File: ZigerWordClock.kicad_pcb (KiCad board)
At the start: 2 copper layers, 237 x 237 mm, 19 parts, among them U1 BTF-5V-060L-B_SK9822_LED_Stri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, U10 BTF-5V-060L-B_SK9822_LED_Stri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, U11 BTF-5V-060L-B_SK9822_LED_Stri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, U12 BTF-5V-060L-B_SK9822_LED_Stri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, U13 BTF-5V-060L-B_SK9822_LED_Stri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, U14 BTF-5V-060L-B_SK9822_LED_Stri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, U15 BTF-5V-060L-B_SK9822_LED_Stri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, U16 BTF-5V-060L-B_SK9822_LED_Stri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, U17 BH1750, U18 LILYGO(R)_TTGO_T8_ESP32-S2_V1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, U19 LevelShifter, U2 BTF-5V-060L-B_SK9822_LED_Stri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, U3 BTF-5V-060L-B_SK9822_LED_Stri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, U4 BTF-5V-060L-B_SK9822_LED_Stri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, U5 BTF-5V-060L-B_SK9822_LED_Stri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, U6 BTF-5V-060L-B_SK9822_LED_Stri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, U7 BTF-5V-060L-B_SK9822_LED_Stri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, U8 BTF-5V-060L-B_SK9822_LED_Stri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, U9 BTF-5V-060L-B_SK9822_LED_Stri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

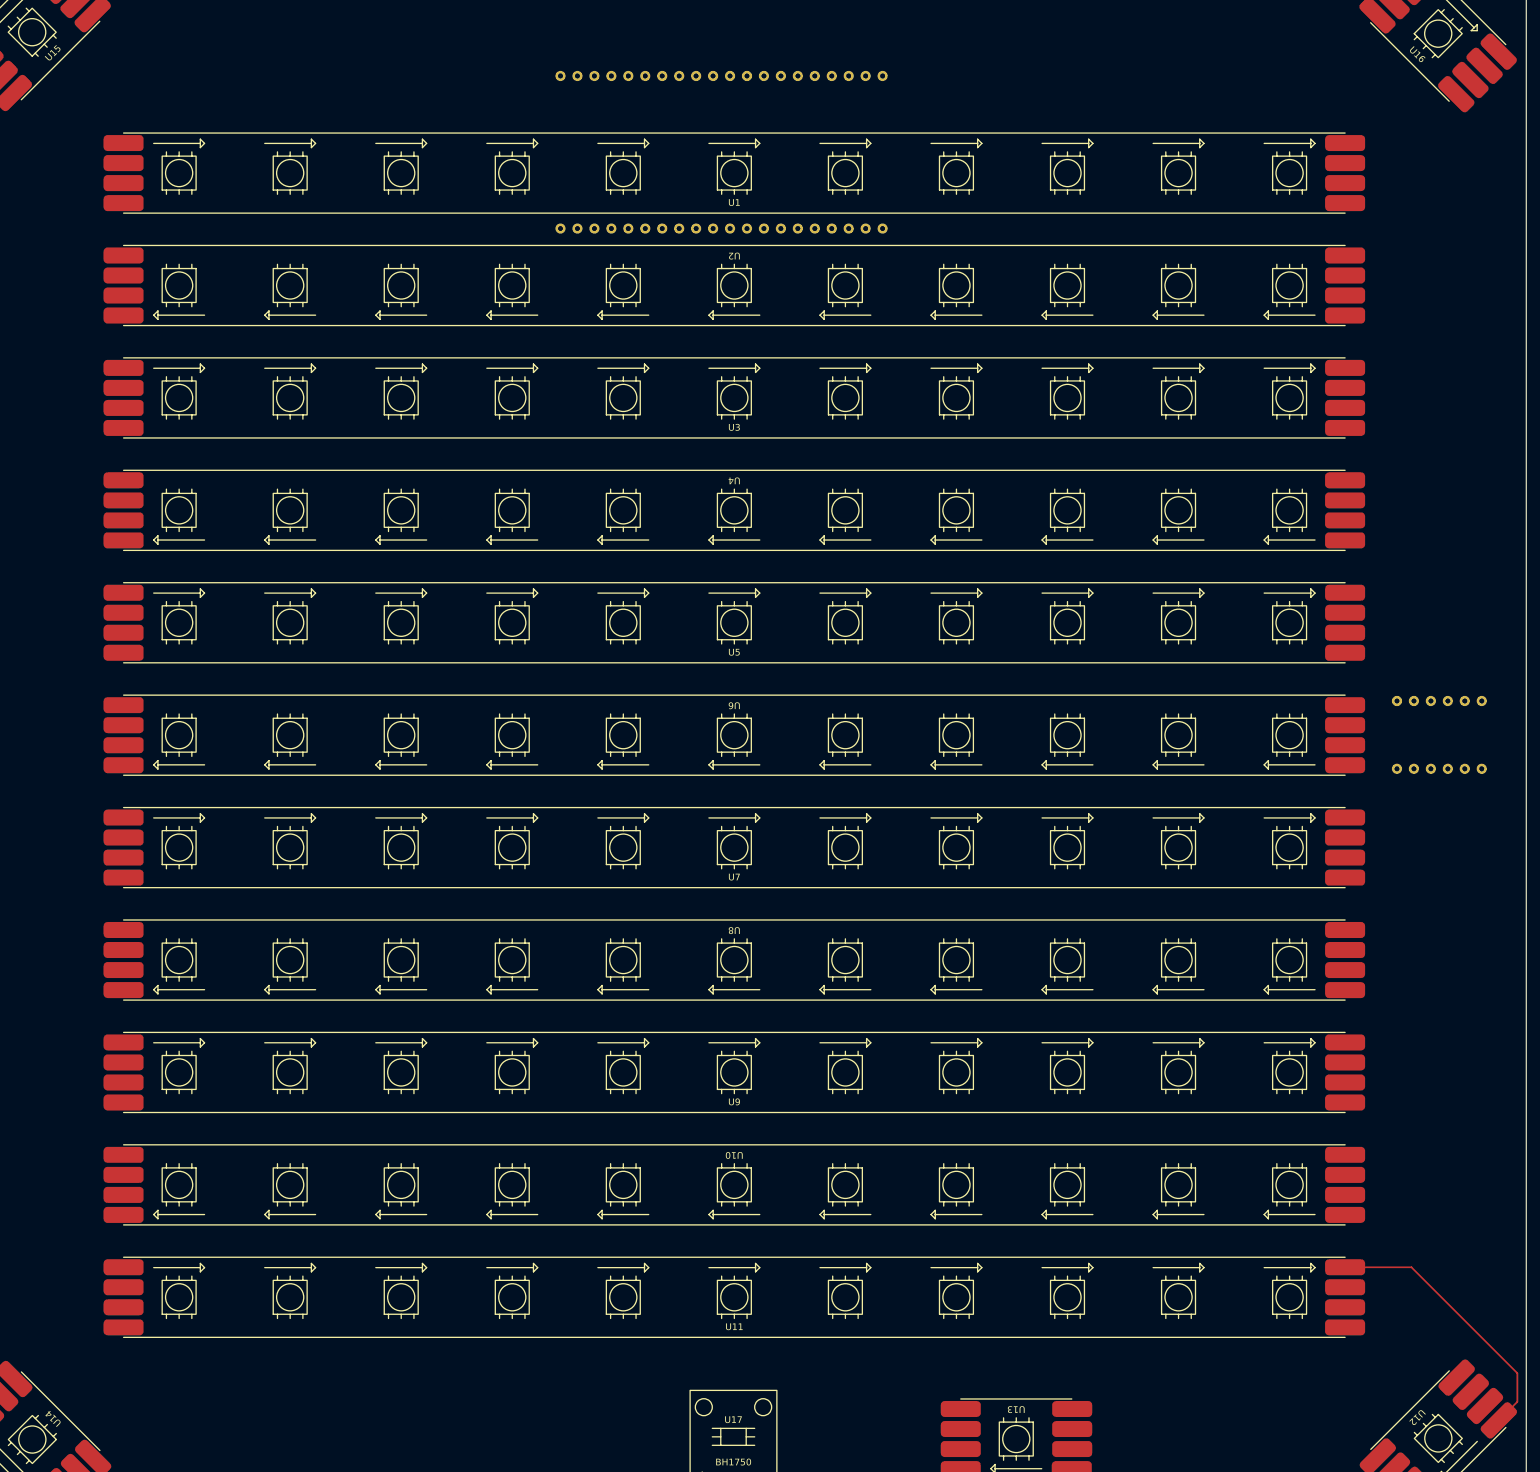
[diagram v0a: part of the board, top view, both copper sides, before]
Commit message: Pins fixed in library
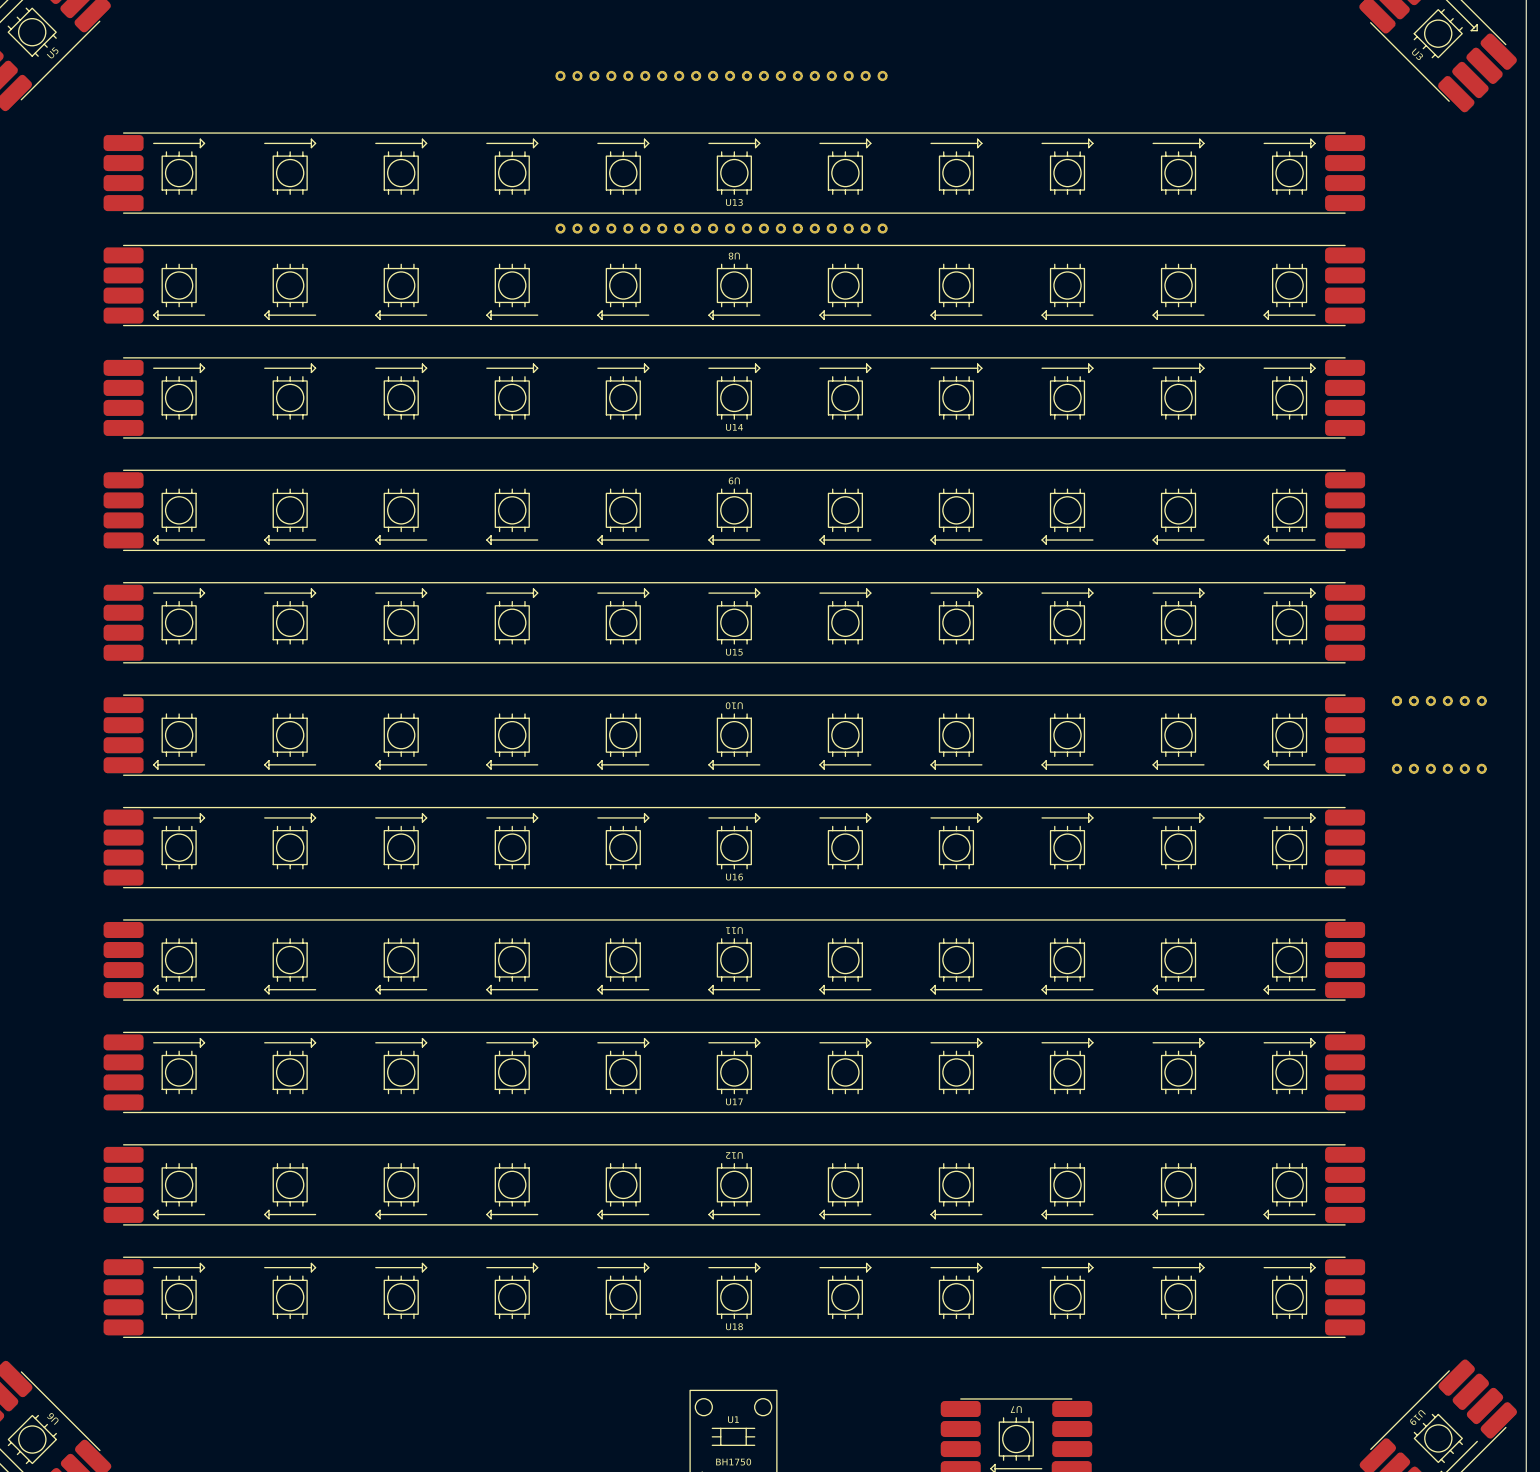
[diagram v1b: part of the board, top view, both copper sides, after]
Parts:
- renumbered U17 to U1, U6 to U10, U8 to U11, U10 to U12, U1 to U13, U3 to U14, U5 to U15, U7 to U16, U9 to U17, U11 to U18, U12 to U19, U18 to U2, U16 to U3, U19 to U4, U15 to U5, U14 to U6, U13 to U7, U2 to U8, U4 to U9
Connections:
- U1 pad ADDR: (no net) -> GND
- U1 pad GND: (no net) -> GND
- U1 pad SCL: (no net) -> Net-(U1-PadSCL)
- U1 pad SDA: (no net) -> Net-(U1-PadSDA)
- U1 pad VCC: (no net) -> unconnected-(U1-PadVCC)
- U10 pad CI: (no net) -> Net-(U10-PadCI)
- U10 pad CO: (no net) -> Net-(U10-PadCO)
- U10 pad DI: (no net) -> Net-(U10-PadDI)
- U10 pad DO: (no net) -> Net-(U10-PadDO)
- U11 pad CI: (no net) -> Net-(U11-PadCI)
- U11 pad CO: (no net) -> Net-(U11-PadCO)
- U11 pad DI: (no net) -> Net-(U11-PadDI)
- U11 pad DO: (no net) -> Net-(U11-PadDO)
- U12 pad CI: (no net) -> Net-(U12-PadCI)
- U12 pad CO: (no net) -> Net-(U12-PadCO)
- U12 pad DI: (no net) -> Net-(U12-PadDI)
- U12 pad DO: (no net) -> Net-(U12-PadDO)
- U13 pad CI: (no net) -> CI
- U13 pad CO: (no net) -> Net-(U13-PadCO)
- U13 pad DI: (no net) -> DI
- U13 pad DO: (no net) -> Net-(U13-PadDO)
- U14 pad CI: (no net) -> Net-(U14-PadCI)
- U14 pad CO: (no net) -> Net-(U14-PadCO)
- U14 pad DI: (no net) -> Net-(U14-PadDI)
- U14 pad DO: (no net) -> Net-(U14-PadDO)
- U15 pad CI: (no net) -> Net-(U15-PadCI)
- U15 pad CO: (no net) -> Net-(U10-PadCI)
- U15 pad DI: (no net) -> Net-(U15-PadDI)
- U15 pad DO: (no net) -> Net-(U10-PadDI)
- U16 pad CI: (no net) -> Net-(U10-PadCO)
- U16 pad CO: (no net) -> Net-(U11-PadCI)
- U16 pad DI: (no net) -> Net-(U10-PadDO)
- U16 pad DO: (no net) -> Net-(U11-PadDI)
- U17 pad CI: (no net) -> Net-(U11-PadCO)
- U17 pad CO: (no net) -> Net-(U12-PadCI)
- U17 pad DI: (no net) -> Net-(U11-PadDO)
- U17 pad DO: (no net) -> Net-(U12-PadDI)
- U18 pad CI: (no net) -> Net-(U12-PadCO)
- U18 pad CO: (no net) -> Net-(U18-PadCO)
- U18 pad DI: (no net) -> Net-(U12-PadDO)
- U18 pad DO: (no net) -> Net-(U18-PadDO)
- U19 pad CI: (no net) -> Net-(U18-PadCO)
- U19 pad CO: (no net) -> Net-(U19-PadCO)
- U19 pad DI: (no net) -> Net-(U18-PadDO)
- U19 pad DO: (no net) -> Net-(U19-PadDO)
- U2 pad 1: (no net) -> unconnected-(U2-Pad1)
- U2 pad 10: (no net) -> unconnected-(U2-Pad10)
- U2 pad 14: (no net) -> unconnected-(U2-Pad14)
- U2 pad 2: (no net) -> unconnected-(U2-Pad2)
- U2 pad 21: (no net) -> +5V
- U2 pad 22: (no net) -> +5V
- U2 pad 23: (no net) -> GND
- U2 pad 24: (no net) -> GND
- U2 pad 25: (no net) -> unconnected-(U2-Pad25)
- U2 pad 26: (no net) -> unconnected-(U2-Pad26)
- U2 pad 27: (no net) -> unconnected-(U2-Pad27)
- U2 pad 28: (no net) -> unconnected-(U2-Pad28)
- U2 pad 29: (no net) -> unconnected-(U2-Pad29)
- U2 pad 3: (no net) -> unconnected-(U2-Pad3)
- U2 pad 30: (no net) -> unconnected-(U2-Pad30)
- U2 pad 31: (no net) -> unconnected-(U2-Pad31)
- U2 pad 32: (no net) -> unconnected-(U2-Pad32)
- U2 pad 4: (no net) -> unconnected-(U2-Pad4)
- U2 pad 5: (no net) -> unconnected-(U2-Pad5)
- U2 pad 6: (no net) -> unconnected-(U2-Pad6)
- U2 pad 7: (no net) -> unconnected-(U2-Pad7)
- U2 pad 8: (no net) -> unconnected-(U2-Pad8)
- U2 pad 9: (no net) -> unconnected-(U2-Pad9)
- U3 pad CI: (no net) -> Net-(U3-PadCI)
- U3 pad CO: (no net) -> unconnected-(U3-PadCO)
- U3 pad DI: (no net) -> Net-(U3-PadDI)
- U3 pad DO: (no net) -> unconnected-(U3-PadDO)
- U4 pad 3: unconnected-(U19-Pad3) -> +5V
- U4 pad 4: unconnected-(U19-Pad4) -> GND
- U4 pad 5: unconnected-(U19-Pad5) -> DI
- U4 pad 6: unconnected-(U19-Pad6) -> CI
- U4 pad 9: unconnected-(U19-Pad9) -> GND
- U5 pad CI: (no net) -> Net-(U5-PadCI)
- U5 pad CO: (no net) -> Net-(U3-PadCI)
- U5 pad DI: (no net) -> Net-(U5-PadDI)
- U5 pad DO: (no net) -> Net-(U3-PadDI)
- U6 pad CI: (no net) -> Net-(U6-PadCI)
- U6 pad CO: (no net) -> Net-(U5-PadCI)
- U6 pad DI: (no net) -> Net-(U6-PadDI)
- U6 pad DO: (no net) -> Net-(U5-PadDI)
- U7 pad CI: (no net) -> Net-(U19-PadCO)
- U7 pad CO: (no net) -> Net-(U6-PadCI)
- U7 pad DI: (no net) -> Net-(U19-PadDO)
- U7 pad DO: (no net) -> Net-(U6-PadDI)
- U8 pad CI: (no net) -> Net-(U13-PadCO)
- U8 pad CO: (no net) -> Net-(U14-PadCI)
- U8 pad DI: (no net) -> Net-(U13-PadDO)
- U8 pad DO: (no net) -> Net-(U14-PadDI)
- U9 pad CI: (no net) -> Net-(U14-PadCO)
- U9 pad CO: (no net) -> Net-(U15-PadCI)
- U9 pad DI: (no net) -> Net-(U14-PadDO)
- U9 pad DO: (no net) -> Net-(U15-PadDI)
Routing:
- net (no net): track 40.6 -> 0.00 mm

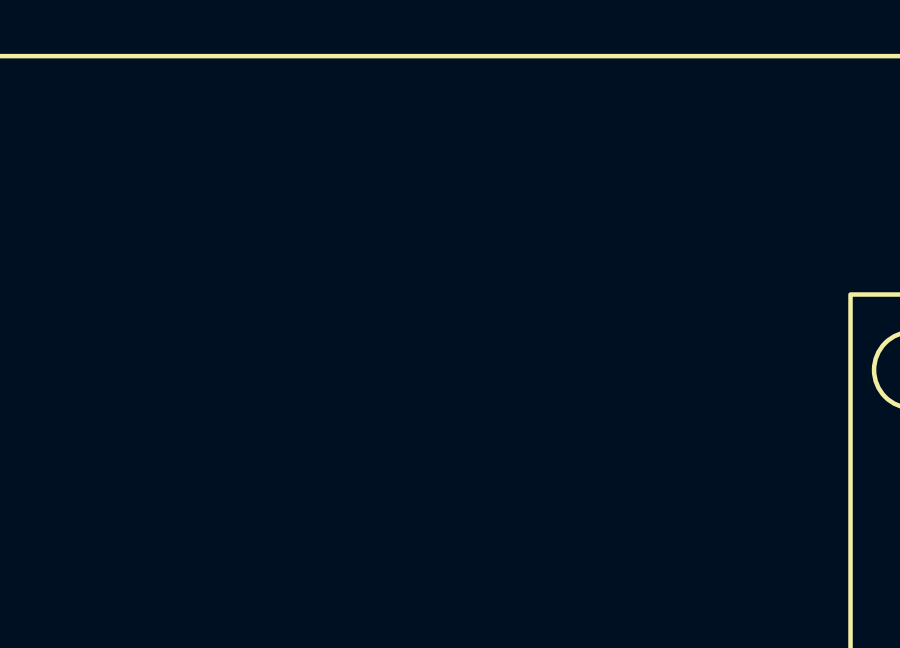
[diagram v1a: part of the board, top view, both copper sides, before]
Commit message: Fixed library and missing footprints for i2c resistors
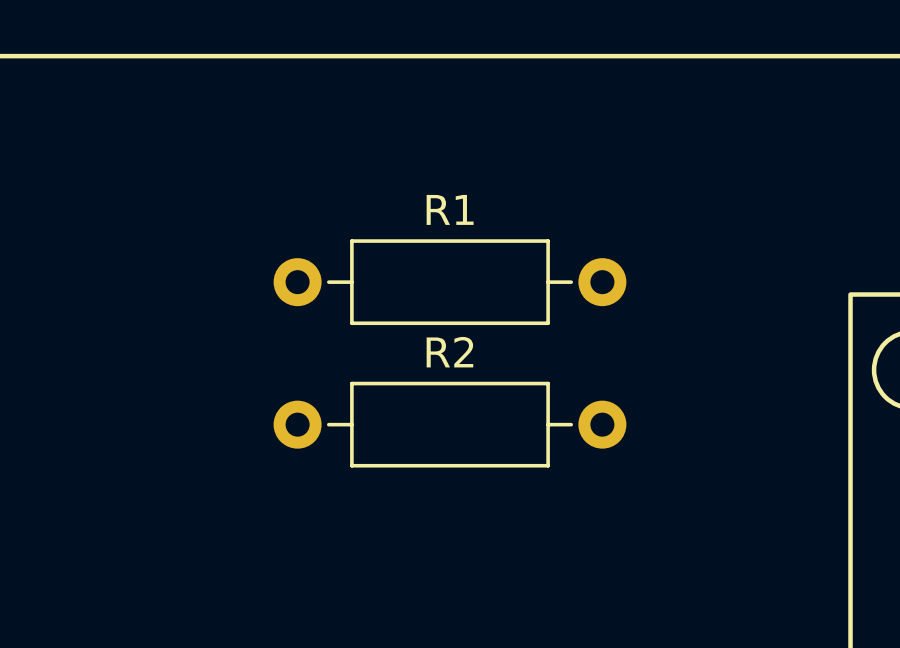
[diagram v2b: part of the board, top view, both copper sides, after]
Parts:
- added R1: R, Resistor_THT:R_Axial_DIN0207_L6.3mm_D2.5mm_P10.16mm_Horizontal, F.Cu at (135.1, 247.3)
- added R2: R, Resistor_THT:R_Axial_DIN0207_L6.3mm_D2.5mm_P10.16mm_Horizontal, F.Cu at (135.1, 252.0)
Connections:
- U10 pad 5V_2: (no net) -> +5V
- U11 pad 5V_2: (no net) -> +5V
- U12 pad 5V_2: (no net) -> +5V
- U13 pad 5V_2: (no net) -> +5V
- U14 pad 5V_2: (no net) -> +5V
- U15 pad 5V_2: (no net) -> +5V
- U16 pad 5V_2: (no net) -> +5V
- U17 pad 5V_2: (no net) -> +5V
- U18 pad 5V_2: (no net) -> +5V
- U8 pad 5V_2: (no net) -> +5V
- U9 pad 5V_2: (no net) -> +5V
